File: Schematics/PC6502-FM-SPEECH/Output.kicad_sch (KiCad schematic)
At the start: 23 parts, among them J2 SJ-3523-SMT-TR, U8 MCP6002-xSN

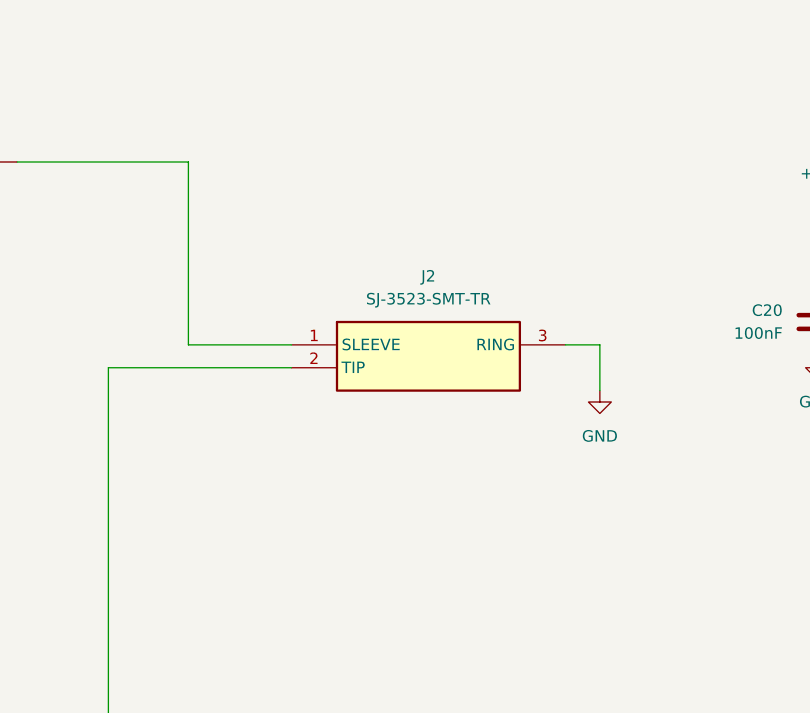
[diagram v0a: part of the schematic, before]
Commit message: Fixed output on FM/Speech card
The ring and sleeve were the wrong way around.
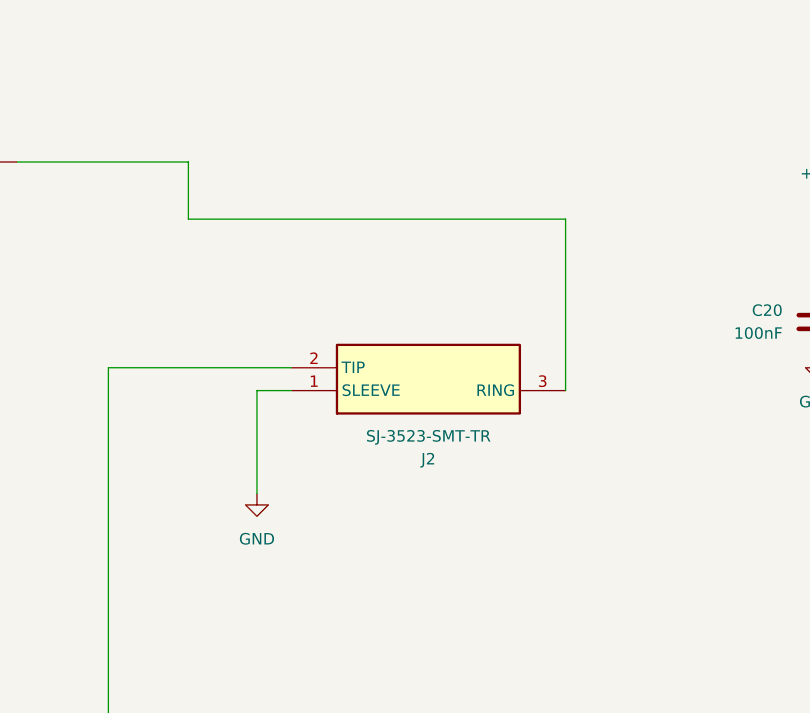
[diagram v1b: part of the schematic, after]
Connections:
- net GND: now also J2.1 (SLEEVE); no longer J2.3 (RING)
- net at C21.2: now also J2.3 (RING); no longer J2.1 (SLEEVE)
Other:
- moved on the sheet: J2
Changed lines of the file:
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@@
+	(wire
+		(pts
+			(xy 218.44 88.9) (xy 176.53 88.9)
+		)
+		(stroke
+			(width 0)
+			(type default)
+		)
+	)
 	(wire
 		(pts
@@
 	(wire
 		(pts
+			(xy 176.53 88.9) (xy 176.53 82.55)
+		)
+		(stroke
+			(width 0)
+			(type default)
+		)
+	)
+	(wire
+		(pts
 			(xy 167.64 105.41) (xy 167.64 168.91)
 		)
@@
 	(wire
 		(pts
-			(xy 187.96 102.87) (xy 176.53 102.87)
-		)
-		(stroke
-			(width 0)
-			(type default)
-		)
-	)
-	(wire
-		(pts
-			(xy 176.53 102.87) (xy 176.53 82.55)
-		)
-		(stroke
-			(width 0)
-			(type default)
-		)
-	)
-	(wire
-		(pts
 			(xy 123.19 115.57) (xy 123.19 128.27)
 		)
@@
 	(wire
 		(pts
-			(xy 222.25 102.87) (xy 222.25 107.95)
+			(xy 184.15 107.95) (xy 184.15 119.38)
 		)
 		(stroke
@@
 	(wire
 		(pts
-			(xy 218.44 102.87) (xy 222.25 102.87)
-		)
-		(stroke
-			(width 0)
-			(type default)
-		)
-	)
-	(wire
-		(pts
 			(xy 73.66 144.78) (xy 73.66 134.62)
 		)
@@
 	(wire
 		(pts
+			(xy 187.96 107.95) (xy 184.15 107.95)
+		)
+		(stroke
+			(width 0)
+			(type default)
+		)
+	)
+	(wire
+		(pts
 			(xy 88.9 29.21) (xy 80.01 29.21)
 		)
@@
 		(pts
 			(xy 104.14 128.27) (xy 109.22 128.27)
+		)
+		(stroke
+			(width 0)
+			(type default)
+		)
+	)
+	(wire
+		(pts
+			(xy 218.44 107.95) (xy 218.44 88.9)
 		)
 		(stroke
@@
 	(symbol
 		(lib_id "power:GND")
-		(at 222.25 107.95 0)
+		(at 184.15 119.38 0)
 		(unit 1)
 		(exclude_from_sim no)
@@
 		(fields_autoplaced yes)
 		(property "Reference" "#PWR064"
-			(at 222.25 114.3 0)
+			(at 184.15 125.73 0)
 			(effects
 				(font
@@
 		)
 		(property "Value" "GND"
-			(at 222.25 113.03 0)
+			(at 184.15 124.46 0)
 			(effects
 				(font
@@
 		)
 		(property "Footprint" ""
-			(at 222.25 107.95 0)
+			(at 184.15 119.38 0)
 			(effects
 				(font
@@
 		)
 		(property "Datasheet" ""
-			(at 222.25 107.95 0)
+			(at 184.15 119.38 0)
 			(effects
 				(font
@@
 		)
 		(property "Description" ""
-			(at 222.25 107.95 0)
+			(at 184.15 119.38 0)
 			(effects
 				(font
@@
 	(symbol
 		(lib_id "SJ-3523-SMT-TR:SJ-3523-SMT-TR")
-		(at 187.96 102.87 0)
+		(at 187.96 107.95 0)
+		(mirror x)
 		(unit 1)
 		(exclude_from_sim no)
@@
 		(on_board yes)
 		(dnp no)
-		(fields_autoplaced yes)
 		(property "Reference" "J2"
-			(at 203.2 95.25 0)
+			(at 203.2 115.57 0)
 			(effects
 				(font
@@
 		)
 		(property "Value" "SJ-3523-SMT-TR"
-			(at 203.2 97.79 0)
+			(at 203.2 113.03 0)
 			(effects
 				(font
@@
 		)
 		(property "Footprint" "SJ-3523-SMT-TR:SJ3523SMTTR"
-			(at 214.63 197.79 0)
+			(at 214.63 13.03 0)
 			(effects
 				(font
@@
 		)
 		(property "Datasheet" "https://www.sameskydevices.com/product/resource/supplyframepdf/sj-352x-smt.pdf"
-			(at 214.63 297.79 0)
+			(at 214.63 -86.97 0)
 			(effects
 				(font
@@
 		)
 		(property "Description" "3.5 mm, Stereo, Right Angle, Surface Mount (SMT), 3 Conductors, 0 Internal Switches, Audio Jack Connector"
-			(at 187.96 102.87 0)
+			(at 187.96 107.95 0)
 			(effects
 				(font
@@
 		)
 		(property "Height" "5.2"
-			(at 214.63 497.79 0)
+			(at 214.63 -286.97 0)
 			(effects
 				(font
@@
 		)
 		(property "Mouser Part Number" "490-SJ-3523-SMT-TR"
-			(at 214.63 597.79 0)
+			(at 214.63 -386.97 0)
 			(effects
 				(font
@@
 		)
 		(property "Mouser Price/Stock" "https://www.mouser.co.uk/ProductDetail/CUI-Devices/SJ-3523-SMT-TR?qs=WyjlAZoYn51zOHzJ3r4ZRA%3D%3D"
-			(at 214.63 697.79 0)
+			(at 214.63 -486.97 0)
 			(effects
 				(font
@@
 		)
 		(property "Manufacturer_Name" "Same Sky"
-			(at 214.63 797.79 0)
+			(at 214.63 -586.97 0)
 			(effects
 				(font
@@
 		)
 		(property "Manufacturer_Part_Number" "SJ-3523-SMT-TR"
-			(at 214.63 897.79 0)
-			(effects
-				(font
+			(at 214.63 -686.97 0)
+			(effects
+				(font
